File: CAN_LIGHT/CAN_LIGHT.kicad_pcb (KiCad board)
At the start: 2 copper layers, 135.5 x 115.4 mm, 94 parts, among them IC1 MSPM0C1103SDDFR, J1 Conn_ARM_SWD_TagConnect_TC2030

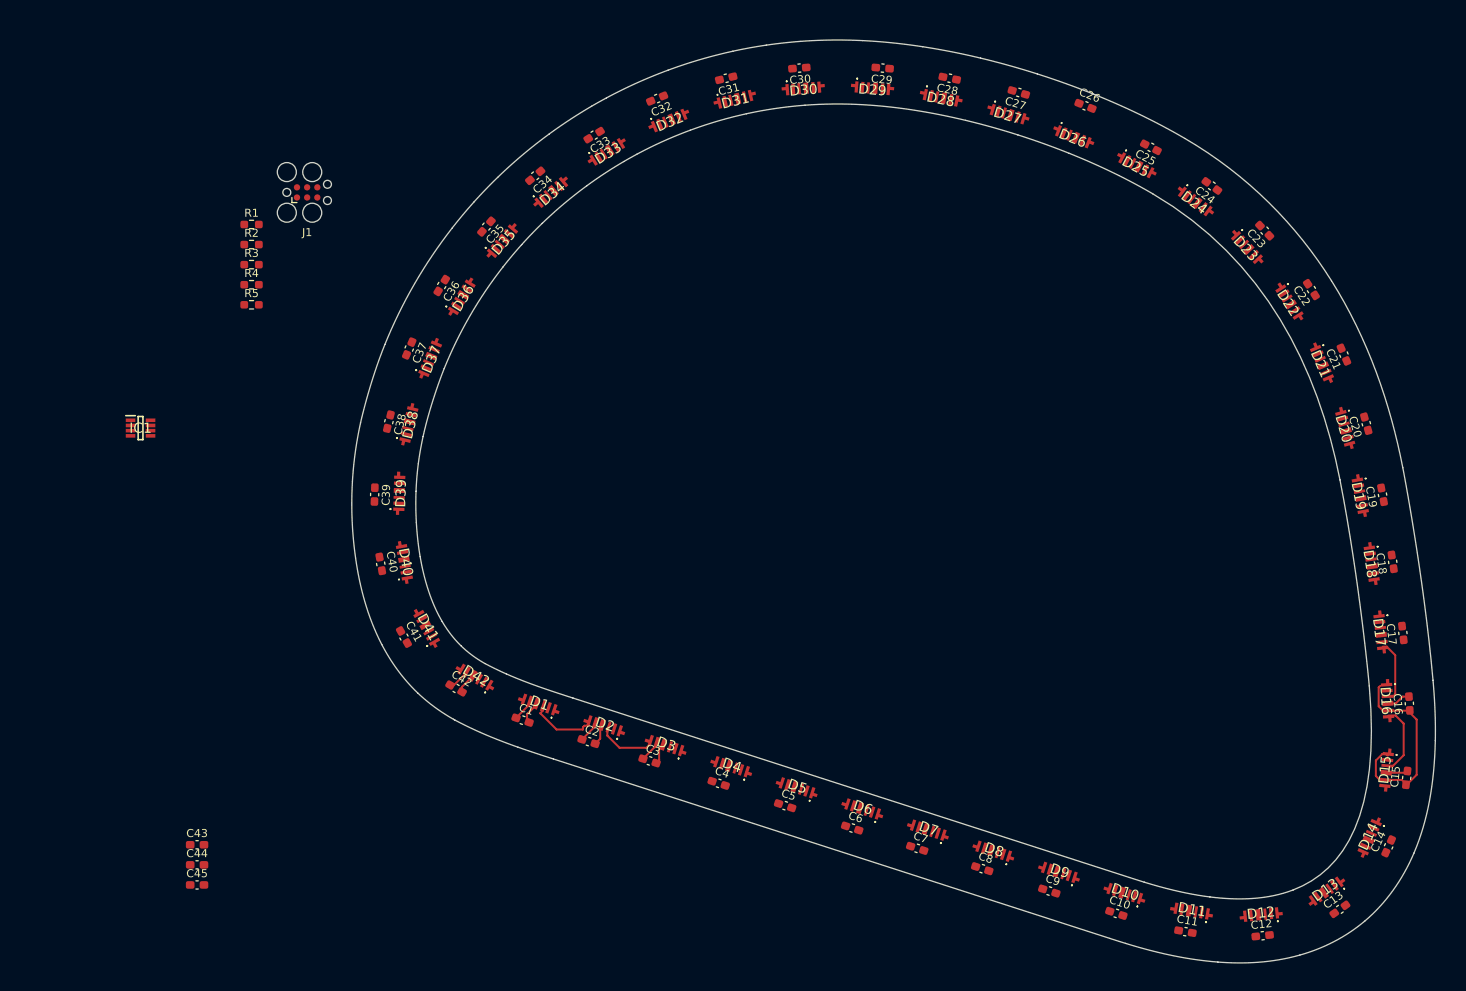
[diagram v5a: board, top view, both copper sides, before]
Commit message: Route several LEDs
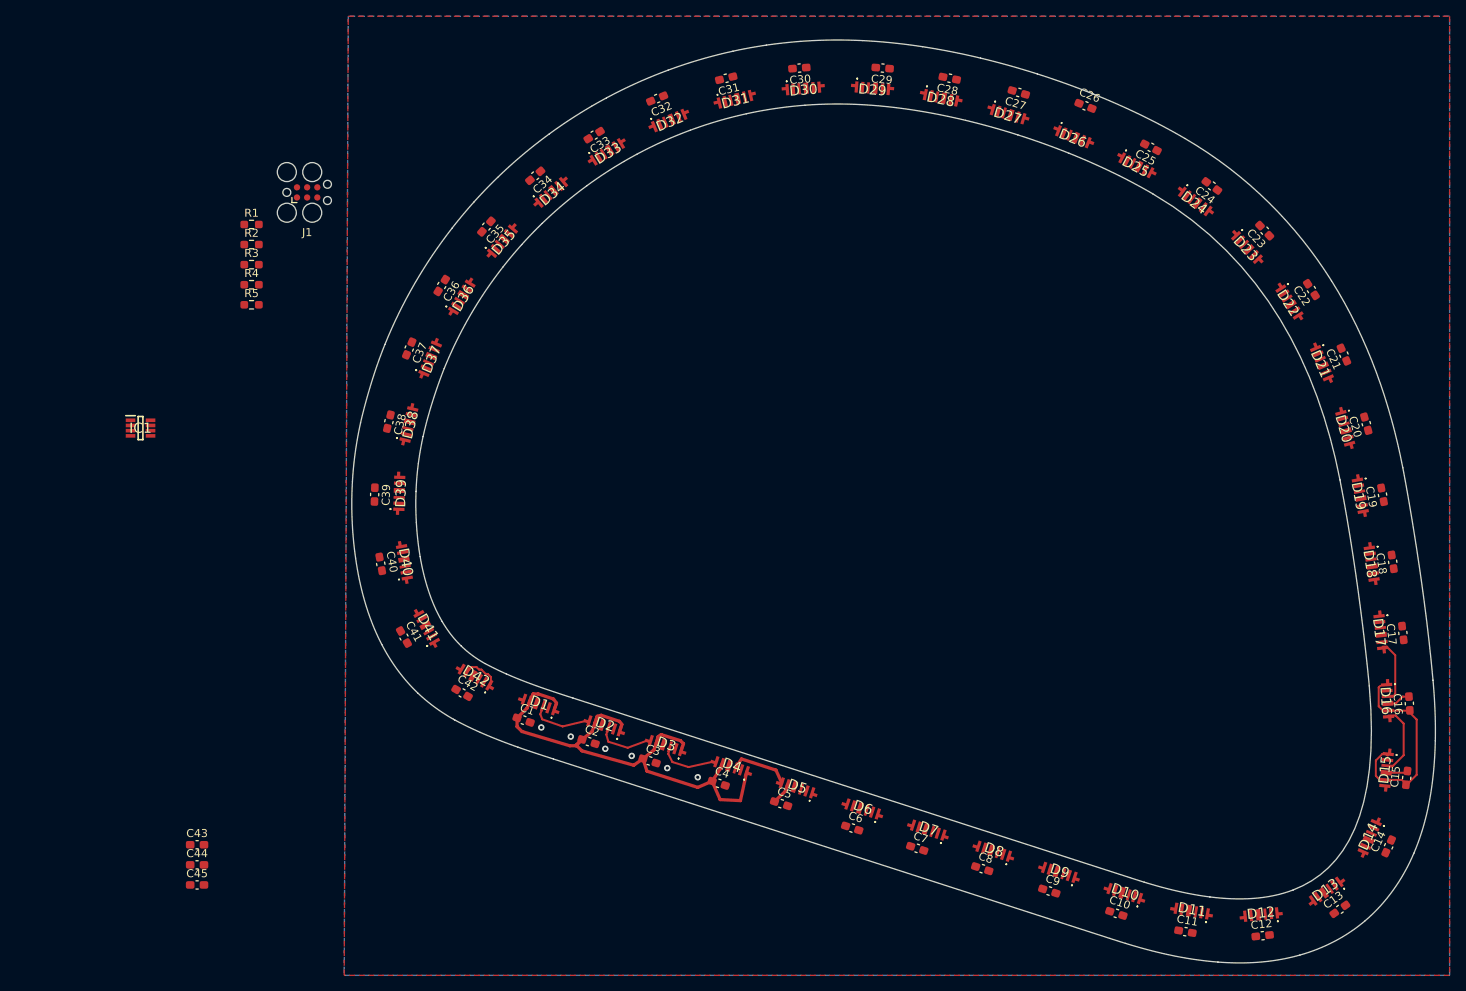
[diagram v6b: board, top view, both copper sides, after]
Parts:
- moved C42 0.93 mm to (79.8, 109.3)
- moved C5 0.57 mm to (119.6, 123.2)
- moved C1 0.13 mm to (87.4, 112.7)
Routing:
- net +5V: track 36.0 -> 97.9 mm
- net GND: track 16.6 -> 5.71 mm, vias 0 -> 6
- net Net-(D4-DOUT): track 0.00 -> 7.64 mm
- net Net-(D3-DOUT): track 0.00 -> 7.23 mm
- net Net-(D1-DOUT): track 8.23 -> 7.42 mm
- added copper zone on B.Cu, net GND
- added copper zone on F.Cu, net GND

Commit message: Route a large portion of the board
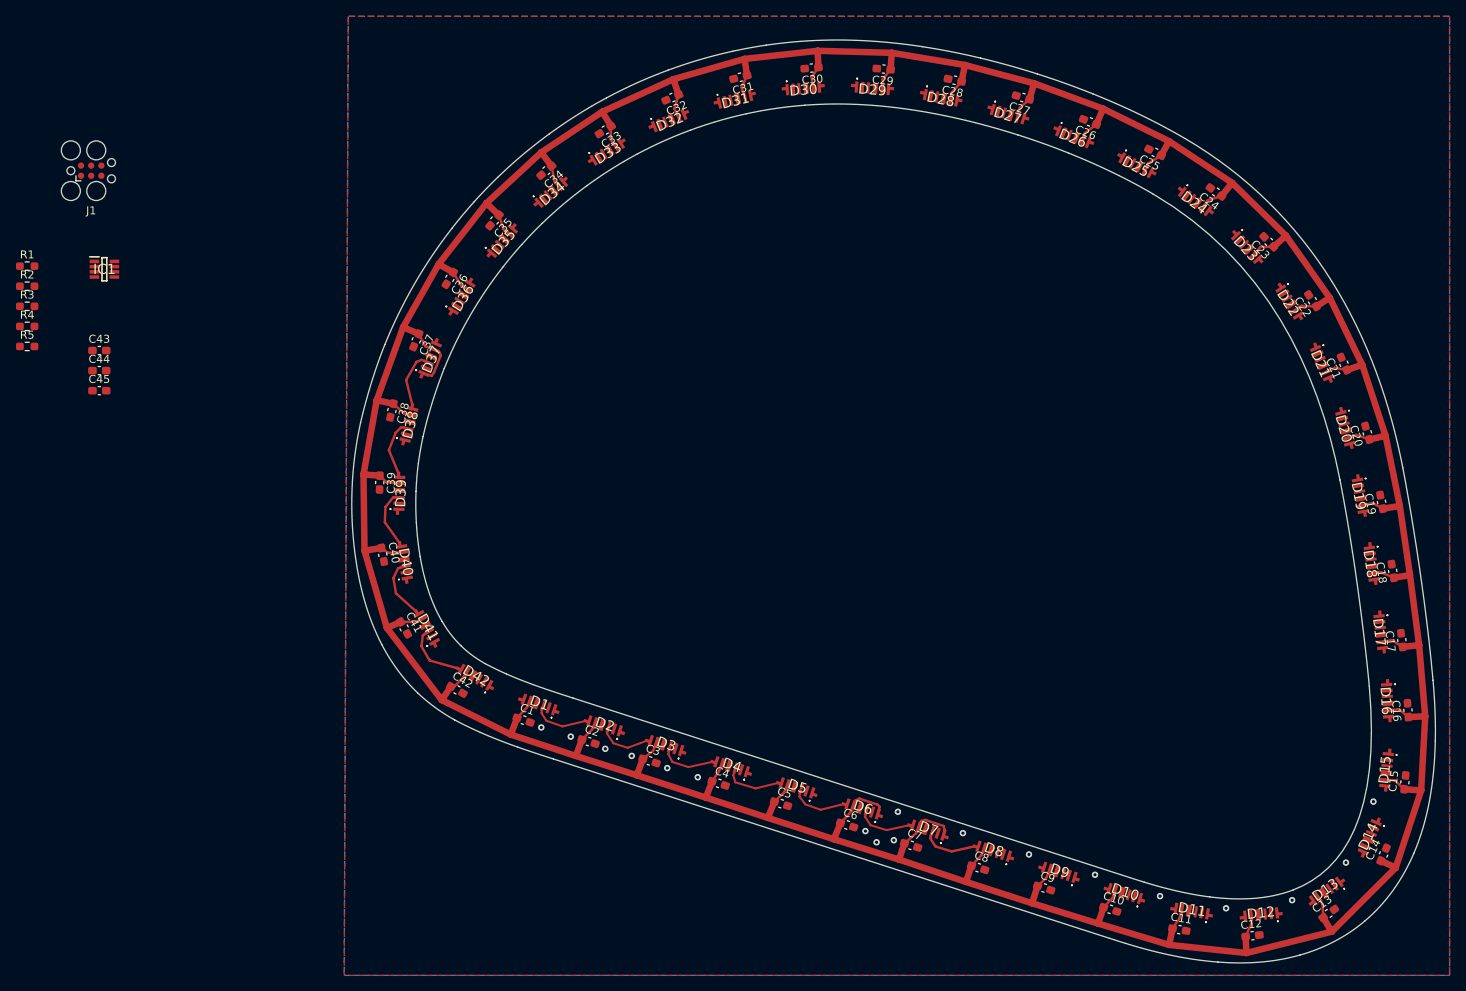
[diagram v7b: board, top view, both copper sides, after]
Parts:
- moved C43 63.0 mm to (34.4, 66.5)
- moved C44 63.0 mm to (34.4, 69.1)
- moved C45 63.0 mm to (34.4, 71.6)
- moved R1 28.5 mm to (25.4, 56.0)
- moved R2 28.5 mm to (25.4, 58.5)
- moved R3 28.5 mm to (25.4, 61.0)
- moved R4 28.5 mm to (25.4, 63.5)
- moved R5 28.5 mm to (25.4, 66.0)
- moved J1 27.1 mm to (33.4, 44.1)
- moved IC1 20.4 mm to (35.1, 56.4)
- moved C26 2.08 mm to (158.2, 38.0), turned to 158.25 degrees
- moved C32 1.91 mm to (106.0, 34.9)
- moved C31 1.78 mm to (114.6, 32.4)
- moved C39 1.63 mm to (69.5, 83.1)
- moved C33 1.53 mm to (97.7, 39.0)
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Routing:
- net +5V: track 97.9 -> 608.6 mm
- net Net-(D15-DOUT): track 8.89 -> 0.00 mm
- net Net-(D16-DOUT): track 8.00 -> 0.00 mm
- net Net-(D41-DOUT): track 0.00 -> 7.97 mm
- net Net-(D40-DOUT): track 0.00 -> 7.58 mm
- net Net-(D37-DOUT): track 0.00 -> 7.47 mm
- net Net-(D39-DOUT): track 0.00 -> 7.40 mm
- net Net-(D38-DOUT): track 0.00 -> 7.35 mm
- net Net-(D7-DOUT): track 0.00 -> 7.17 mm
- net Net-(D5-DOUT): track 0.00 -> 7.15 mm
- net Net-(D6-DOUT): track 0.00 -> 7.08 mm
- net GND: track 5.71 -> 0.00 mm, vias 6 -> 18

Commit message: Finish top layer LED routing
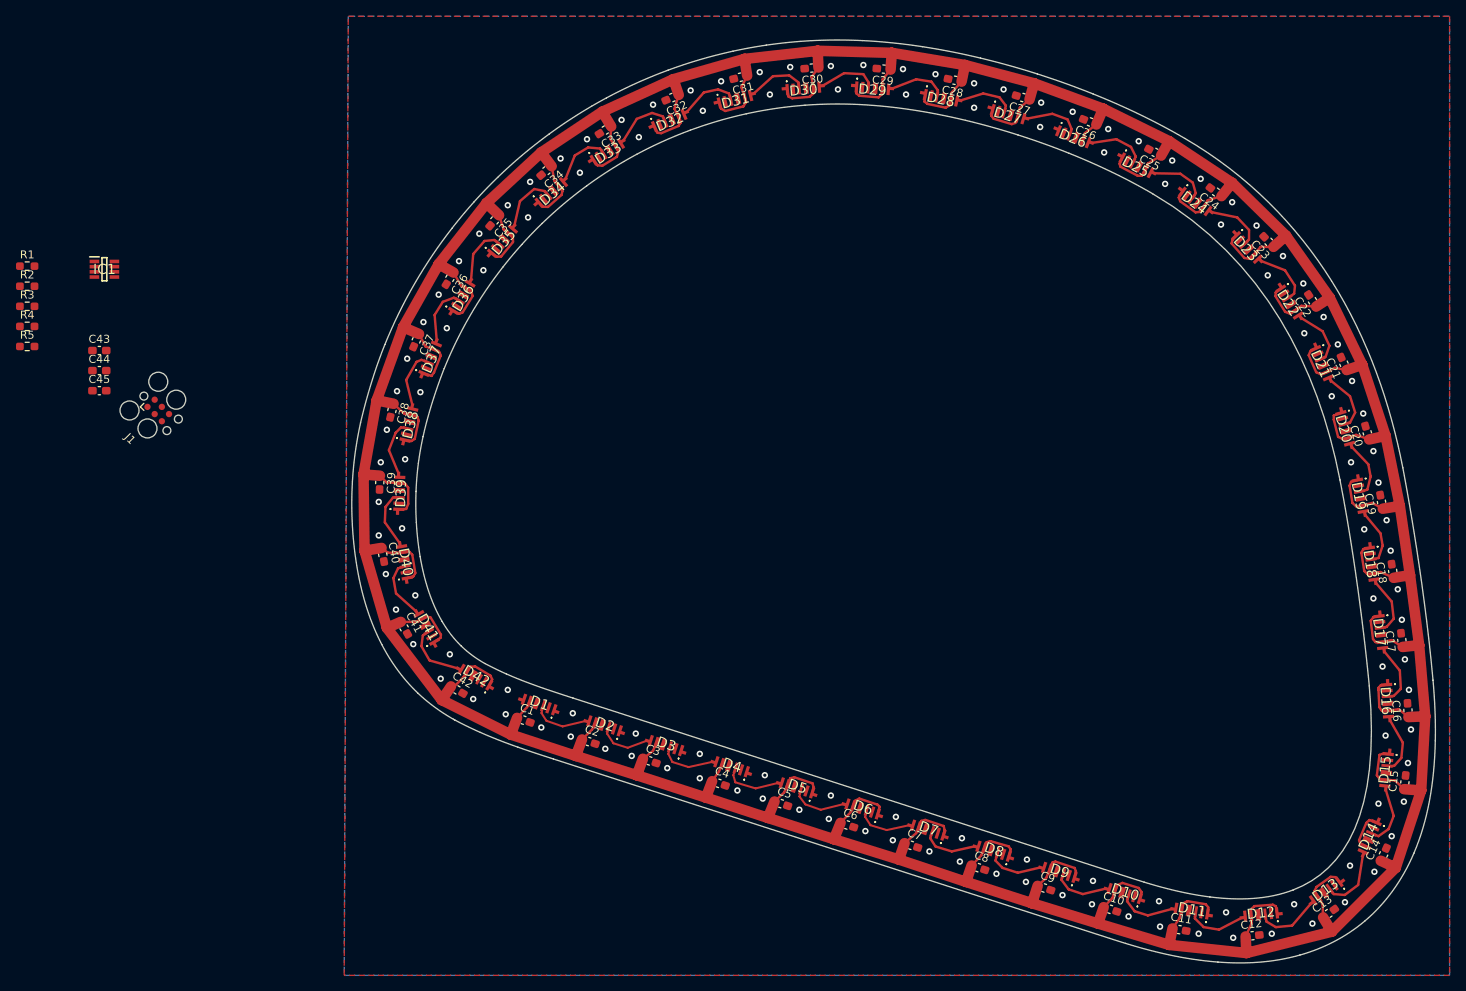
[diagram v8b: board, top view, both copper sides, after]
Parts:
- moved J1 31.1 mm to (41.8, 74.0), turned to -45 degrees
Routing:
- net +5V: track 608.6 -> 776.6 mm
- net Net-(D13-DOUT): track 0.00 -> 8.04 mm
- net Net-(D12-DOUT): track 0.00 -> 7.98 mm
- net Net-(D14-DOUT): track 0.00 -> 7.70 mm
- net Net-(D22-DOUT): track 0.00 -> 7.56 mm
- net Net-(D11-DOUT): track 0.00 -> 7.52 mm
- net Net-(D30-DOUT): track 0.00 -> 7.51 mm
- net Net-(D35-DOUT): track 0.00 -> 7.51 mm
- net Net-(D23-DOUT): track 0.00 -> 7.48 mm
- net Net-(D34-DOUT): track 0.00 -> 7.46 mm
- net Net-(D16-DOUT): track 0.00 -> 7.43 mm
- net Net-(D25-DOUT): track 0.00 -> 7.43 mm
- net Net-(D32-DOUT): track 0.00 -> 7.43 mm
- net Net-(D24-DOUT): track 0.00 -> 7.42 mm
- net Net-(D33-DOUT): track 0.00 -> 7.41 mm
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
